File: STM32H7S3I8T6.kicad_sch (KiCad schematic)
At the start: 48 parts, among them IC5 STM32H7S3I8T6 LQFP 176, Y1 ECS-3225SMV-240-FP-TR

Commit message: Update
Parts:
- removed R6: 33R, Resistor_SMD:R_0603_1608Metric, symbol Device:R
- removed RN12: 33R, Resistor_SMD:R_Array_Convex_4x0402, symbol Device:R_Pack04
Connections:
- net PA3_I2S6_MCK_R is gone; now on net PA3_I2S6_MCK: IC5.39 (PA3)
- net PA4_I2S1_WS_R is gone; now on net PA4_I2S1_WS: IC5.42 (PA4)
- net PA5_I2S1_C_R is gone; now on net PA5_I2S1_CK: IC5.43 (PA5)
- net PA7_I2S6_SDO_R is gone; now on net PA7_I2S6_SDO: IC5.45 (PA7)
- no-connect marks 27 -> 25
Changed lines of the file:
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@@
 	)
 	(no_connect
-		(at 85.09 204.47)
-	)
-	(no_connect
 		(at 220.98 54.61)
 	)
@@
 	)
 	(no_connect
-		(at 95.25 204.47)
-	)
-	(no_connect
 		(at 154.94 129.54)
 	)
@@
 	(wire
 		(pts
-			(xy 134.62 232.41) (xy 162.56 232.41)
-		)
-		(stroke
-			(width 0)
-			(type default)
-		)
-	)
-	(wire
-		(pts
 			(xy 241.3 17.78) (xy 241.3 21.59)
 		)
@@
 	(wire
 		(pts
-			(xy 128.27 201.93) (xy 95.25 201.93)
-		)
-		(stroke
-			(width 0)
-			(type default)
-		)
-	)
-	(wire
-		(pts
 			(xy 27.94 193.04) (xy 27.94 194.31)
 		)
@@
 	(wire
 		(pts
-			(xy 95.25 209.55) (xy 133.35 209.55)
-		)
-		(stroke
-			(width 0)
-			(type default)
-		)
-	)
-	(wire
-		(pts
 			(xy 69.85 154.94) (xy 68.58 154.94)
 		)
@@
 	(wire
 		(pts
-			(xy 95.25 207.01) (xy 130.81 207.01)
-		)
-		(stroke
-			(width 0)
-			(type default)
-		)
-	)
-	(wire
-		(pts
 			(xy 279.4 149.86) (xy 325.12 149.86)
 		)
@@
 	(wire
 		(pts
-			(xy 101.6 232.41) (xy 127 232.41)
+			(xy 101.6 232.41) (xy 162.56 232.41)
 		)
 		(stroke
@@
 	(wire
 		(pts
-			(xy 68.58 209.55) (xy 85.09 209.55)
+			(xy 68.58 209.55) (xy 133.35 209.55)
 		)
 		(stroke
@@
 	(wire
 		(pts
-			(xy 68.58 207.01) (xy 85.09 207.01)
+			(xy 68.58 207.01) (xy 130.81 207.01)
 		)
 		(stroke
@@
 	(wire
 		(pts
-			(xy 68.58 201.93) (xy 85.09 201.93)
+			(xy 68.58 201.93) (xy 128.27 201.93)
 		)
 		(stroke
@@
 		)
 	)
-	(label "PA3_I2S6_MCK_R"
-		(at 130.81 193.04 0)
-		(fields_autoplaced yes)
-		(effects
-			(font
-				(size 1.27 1.27)
-			)
-			(justify left bottom)
-		)
-	)
 	(label "PM9"
 		(at 236.22 62.23 90)
@@
 		)
 	)
-	(label "PA5_I2S1_C_R"
-		(at 137.16 203.2 0)
-		(fields_autoplaced yes)
-		(effects
-			(font
-				(size 1.27 1.27)
-			)
-			(justify left bottom)
-		)
-	)
 	(label "FMC_A1"
 		(at 97.79 170.18 0)
@@
 		)
 	)
-	(label "PA4_I2S1_WS_R"
-		(at 137.16 200.66 0)
-		(fields_autoplaced yes)
-		(effects
-			(font
-				(size 1.27 1.27)
-			)
-			(justify left bottom)
-		)
-	)
 	(label "FMC_NCE_R"
 		(at 127 255.27 180)
@@
 		)
 	)
-	(label "PA7_I2S6_SDO_R"
-		(at 146.05 232.41 0)
-		(fields_autoplaced yes)
-		(effects
-			(font
-				(size 1.27 1.27)
-			)
-			(justify left bottom)
-		)
-	)
 	(label "FMC_D13_R"
 		(at 139.7 114.3 0)
@@
 	(symbol
 		(lib_id "Device:R_Pack04")
-		(at 90.17 207.01 270)
-		(unit 1)
-		(exclude_from_sim no)
-		(in_bom yes)
-		(on_board yes)
-		(dnp no)
-		(property "Reference" "RN12"
-			(at 83.058 211.582 90)
-			(effects
-				(font
-					(size 1.27 1.27)
-				)
-				(justify left)
-			)
-		)
-		(property "Value" "33R"
-			(at 93.98 211.582 90)
-			(effects
-				(font
-					(size 1.27 1.27)
-				)
-				(justify left)
-			)
-		)
-		(property "Footprint" "Resistor_SMD:R_Array_Convex_4x0402"
-			(at 90.17 213.995 90)
-			(effects
-				(font
-					(size 1.27 1.27)
-				)
-				(hide yes)
-			)
-		)
-		(property "Datasheet" "~"
-			(at 90.17 207.01 0)
-			(effects
-				(font
-					(size 1.27 1.27)
-				)
-				(hide yes)
-			)
-		)
-		(property "Description" "4 resistor network, parallel topology"
-			(at 90.17 207.01 0)
-			(effects
-				(font
-					(size 1.27 1.27)
-				)
-				(hide yes)
-			)
-		)
-		(pin "2"
-		)
-		(pin "1"
-		)
-		(pin "8"
-		)
-		(pin "4"
-		)
-		(pin "3"
-		)
-		(pin "7"
-		)
-		(pin "5"
-		)
-		(pin "6"
-		)
-		(instances
-			(project "STM32H7_Board"
-				(path "/9b48e30a-b912-4658-a133-1a15707d5b7d/c1266206-99aa-4330-9c51-1a1fe13fdf97"
-					(reference "RN12")
-					(unit 1)
-				)
-			)
-		)
-	)
-	(symbol
-		(lib_id "Device:R_Pack04")
 		(at 90.17 257.81 90)
 		(mirror x)
@@
 					(unit 1)
 				)
-			)
-		)
-	)
-	(symbol
-		(lib_id "Device:R")
-		(at 130.81 232.41 90)
-		(unit 1)
-		(exclude_from_sim no)
-		(in_bom yes)
-		(on_board yes)
-		(dnp no)
-		(property "Reference" "R6"
-			(at 125.984 231.14 90)
-			(effects
-				(font
-					(size 1.27 1.27)
-				)
-			)
-		)
-		(property "Value" "33R"
-			(at 135.636 231.14 90)
-			(effects
-				(font
-					(size 1.27 1.27)
-				)
-			)
-		)
-		(property "Footprint" "Resistor_SMD:R_0603_1608Metric"
-			(at 130.81 234.188 90)
-			(effects
-				(font
-					(size 1.27 1.27)
-				)
-				(hide yes)
-			)
-		)
-		(property "Datasheet" "~"
-			(at 130.81 232.41 0)
-			(effects
-				(font
-					(size 1.27 1.27)
-				)
-				(hide yes)
-			)
-		)
-		(property "Description" "Resistor"
-			(at 130.81 232.41 0)
-			(effects
-				(font
-					(size 1.27 1.27)
-				)
-				(hide yes)
-			)
-		)
-		(pin "1"
-		)
-		(pin "2"
-		)
-		(instances
-			(project "STM32H7_Board"
-				(path "/9b48e30a-b912-4658-a133-1a15707d5b7d/c1266206-99aa-4330-9c51-1a1fe13fdf97"
-					(reference "R6")
-					(unit 1)
-				)

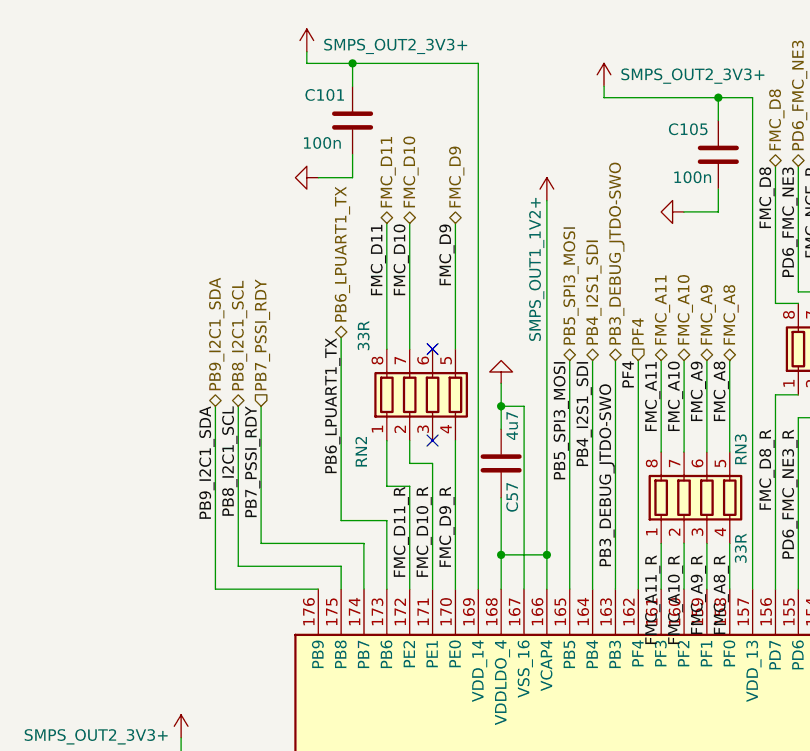
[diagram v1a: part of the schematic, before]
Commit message: Added I2C to the LCD interface
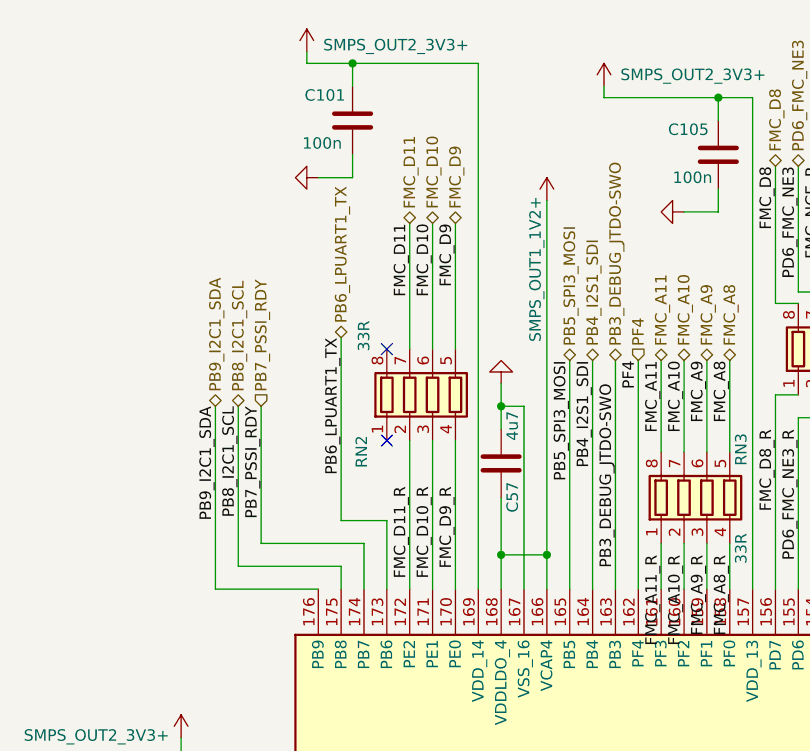
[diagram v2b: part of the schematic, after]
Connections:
- net FMC_D10: now also RN2.6 (R3.2); no longer RN2.7 (R2.2)
- net FMC_D10_R: now also RN2.3 (R3.1); no longer RN2.2 (R2.1)
- net FMC_D11: now also RN2.7 (R2.2); no longer RN2.8 (R1.2)
- net FMC_D11_R: now also RN2.2 (R2.1); no longer RN2.1 (R1.1)
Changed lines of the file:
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@@
 	)
 	(no_connect
-		(at 264.16 270.51)
+		(at 170.18 49.53)
 	)
 	(no_connect
-		(at 175.26 59.69)
+		(at 264.16 270.51)
 	)
 	(no_connect
@@
 	)
 	(no_connect
-		(at 175.26 49.53)
-	)
-	(no_connect
 		(at 220.98 54.61)
 	)
@@
 	)
 	(no_connect
+		(at 170.18 59.69)
+	)
+	(no_connect
 		(at 220.98 44.45)
 	)
@@
 	(wire
 		(pts
-			(xy 170.18 35.56) (xy 170.18 49.53)
-		)
-		(stroke
-			(width 0)
-			(type default)
-		)
-	)
-	(wire
-		(pts
 			(xy 154.94 139.7) (xy 121.92 139.7)
 		)
@@
 	(wire
 		(pts
-			(xy 172.72 62.23) (xy 172.72 59.69)
-		)
-		(stroke
-			(width 0)
-			(type default)
-		)
-	)
-	(wire
-		(pts
 			(xy 139.7 142.24) (xy 154.94 142.24)
 		)
@@
 	(wire
 		(pts
-			(xy 172.72 64.77) (xy 170.18 64.77)
-		)
-		(stroke
-			(width 0)
-			(type default)
-		)
-	)
-	(wire
-		(pts
 			(xy 304.8 205.74) (xy 279.4 205.74)
 		)
@@
 	(wire
 		(pts
+			(xy 172.72 59.69) (xy 172.72 76.2)
+		)
+		(stroke
+			(width 0)
+			(type default)
+		)
+	)
+	(wire
+		(pts
 			(xy 78.74 152.4) (xy 68.58 152.4)
 		)
@@
 	(wire
 		(pts
+			(xy 175.26 59.69) (xy 175.26 76.2)
+		)
+		(stroke
+			(width 0)
+			(type default)
+		)
+	)
+	(wire
+		(pts
 			(xy 101.6 90.17) (xy 105.41 90.17)
 		)
@@
 	(wire
 		(pts
-			(xy 175.26 62.23) (xy 175.26 76.2)
-		)
-		(stroke
-			(width 0)
-			(type default)
-		)
-	)
-	(wire
-		(pts
 			(xy 69.85 154.94) (xy 68.58 154.94)
 		)
@@
 	(wire
 		(pts
-			(xy 172.72 64.77) (xy 172.72 76.2)
-		)
-		(stroke
-			(width 0)
-			(type default)
-		)
-	)
-	(wire
-		(pts
 			(xy 231.14 228.6) (xy 231.14 248.92)
 		)
@@
 	(wire
 		(pts
-			(xy 170.18 64.77) (xy 170.18 59.69)
-		)
-		(stroke
-			(width 0)
-			(type default)
-		)
-	)
-	(wire
-		(pts
 			(xy 128.27 193.04) (xy 128.27 201.93)
 		)
@@
 	(wire
 		(pts
-			(xy 172.72 35.56) (xy 172.72 49.53)
+			(xy 175.26 35.56) (xy 175.26 49.53)
 		)
 		(stroke
@@
 	(wire
 		(pts
-			(xy 175.26 62.23) (xy 172.72 62.23)
-		)
-		(stroke
-			(width 0)
-			(type default)
-		)
-	)
-	(wire
-		(pts
 			(xy 125.73 160.02) (xy 125.73 157.48)
 		)
@@
 	(wire
 		(pts
+			(xy 172.72 35.56) (xy 172.72 49.53)
+		)
+		(stroke
+			(width 0)
+			(type default)
+		)
+	)
+	(wire
+		(pts
 			(xy 215.9 57.15) (xy 215.9 76.2)
 		)
@@
 	)
 	(label "FMC_D10"
-		(at 172.72 35.56 270)
+		(at 175.26 35.56 270)
 		(fields_autoplaced yes)
 		(effects
@@
 	)
 	(label "FMC_D11"
-		(at 170.18 35.56 270)
+		(at 172.72 35.56 270)
 		(fields_autoplaced yes)
 		(effects
@@
 	(hierarchical_label "FMC_D11"
 		(shape bidirectional)
-		(at 170.18 35.56 90)
+		(at 172.72 35.56 90)
 		(fields_autoplaced yes)
 		(effects
@@
 	(hierarchical_label "FMC_D10"
 		(shape bidirectional)
-		(at 172.72 35.56 90)
+		(at 175.26 35.56 90)
 		(fields_autoplaced yes)
 		(effects

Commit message: Update
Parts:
- Y1: value ECS-3225SMV-240-FP-TR -> ECS-3225SMVQ-240-DS-TR
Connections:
- net SMPS_OUT2_3V3+: now also OS3.1 (TRI-STATE)
- no-connect marks 25 -> 24
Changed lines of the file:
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@@
 	)
 	(junction
+		(at 53.34 92.71)
+		(diameter 0)
+		(color 0 0 0 0)
+	)
+	(junction
 		(at 283.21 57.15)
 		(diameter 0)
@@
 	)
 	(no_connect
-		(at 57.15 92.71)
-	)
-	(no_connect
 		(at 259.08 270.51)
 	)
@@
 	(wire
 		(pts
-			(xy 53.34 90.17) (xy 53.34 99.06)
+			(xy 53.34 90.17) (xy 53.34 92.71)
 		)
 		(stroke
@@
 	(wire
 		(pts
+			(xy 53.34 92.71) (xy 53.34 99.06)
+		)
+		(stroke
+			(width 0)
+			(type default)
+		)
+	)
+	(wire
+		(pts
 			(xy 269.24 228.6) (xy 269.24 233.68)
 		)
@@
 	(wire
 		(pts
+			(xy 53.34 92.71) (xy 57.15 92.71)
+		)
+		(stroke
+			(width 0)
+			(type default)
+		)
+	)
+	(wire
+		(pts
 			(xy 218.44 57.15) (xy 215.9 57.15)
 		)
@@
 		)
 		(property "Value" "SMPS_OUT2_3V3+"
-			(at 46.99 108.712 0)
+			(at 42.418 107.696 0)
 			(effects
 				(font
@@
 			)
 		)
-		(property "Value" "ECS-3225SMV-240-FP-TR"
+		(property "Value" "ECS-3225SMVQ-240-DS-TR"
 			(at 52.07 147.32 0)
 			(effects

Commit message: Update
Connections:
- net GND: now also RN7.4 (R4.1), RN7.5 (R4.2)
- no-connect marks 24 -> 22
